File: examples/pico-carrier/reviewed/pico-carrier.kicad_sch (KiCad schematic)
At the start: 9 parts, among them J1 5V IN, J3 GP0-GP15, J4 GP16-GP28, PWR, U1 Pico

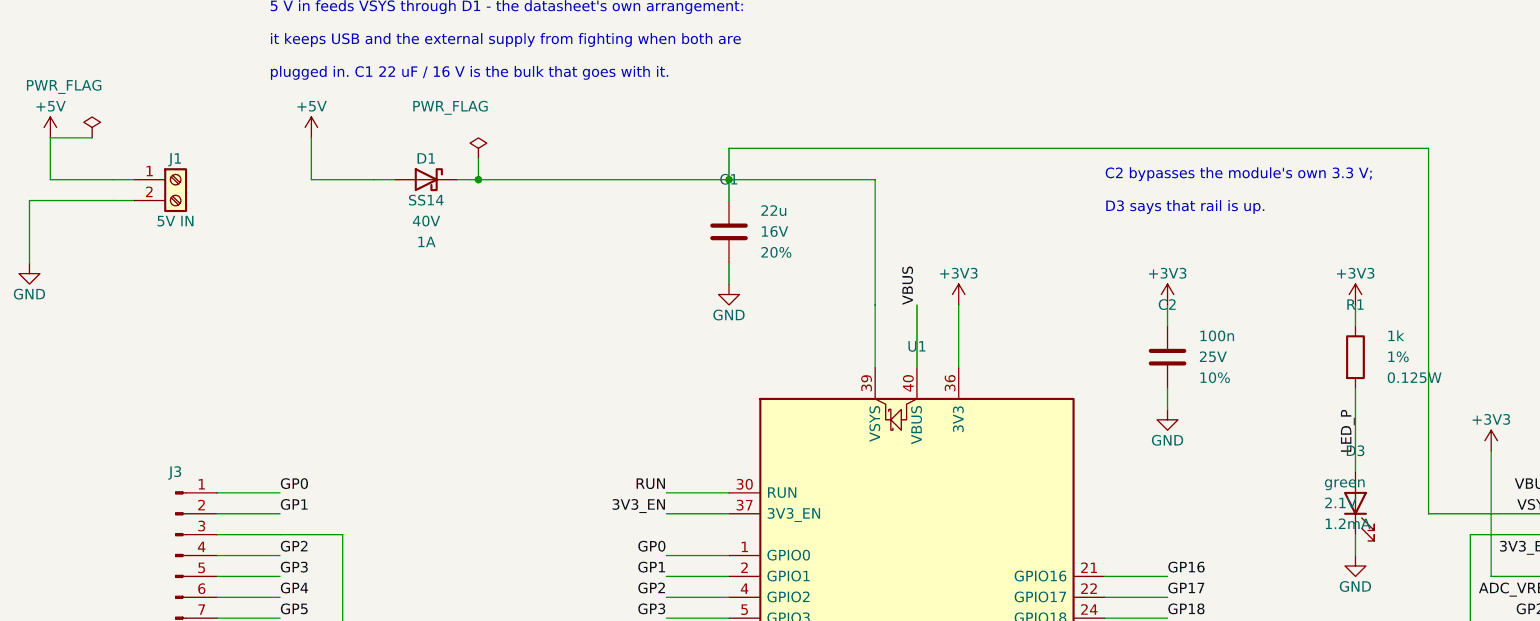
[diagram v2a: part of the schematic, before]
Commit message: Regenerate the four the text and width work changed
Designators and values off the rails they were printed on, power-named
nets at the width their rule asks for, and the buck's feedback ending
on the capacitor pad it senses at.

Co-Authored-By: Claude Fable 5 <noreply@anthropic.com>
Claude-Session: https://claude.ai/code/session_01DUj7Ltu92tWg159mCSacwY
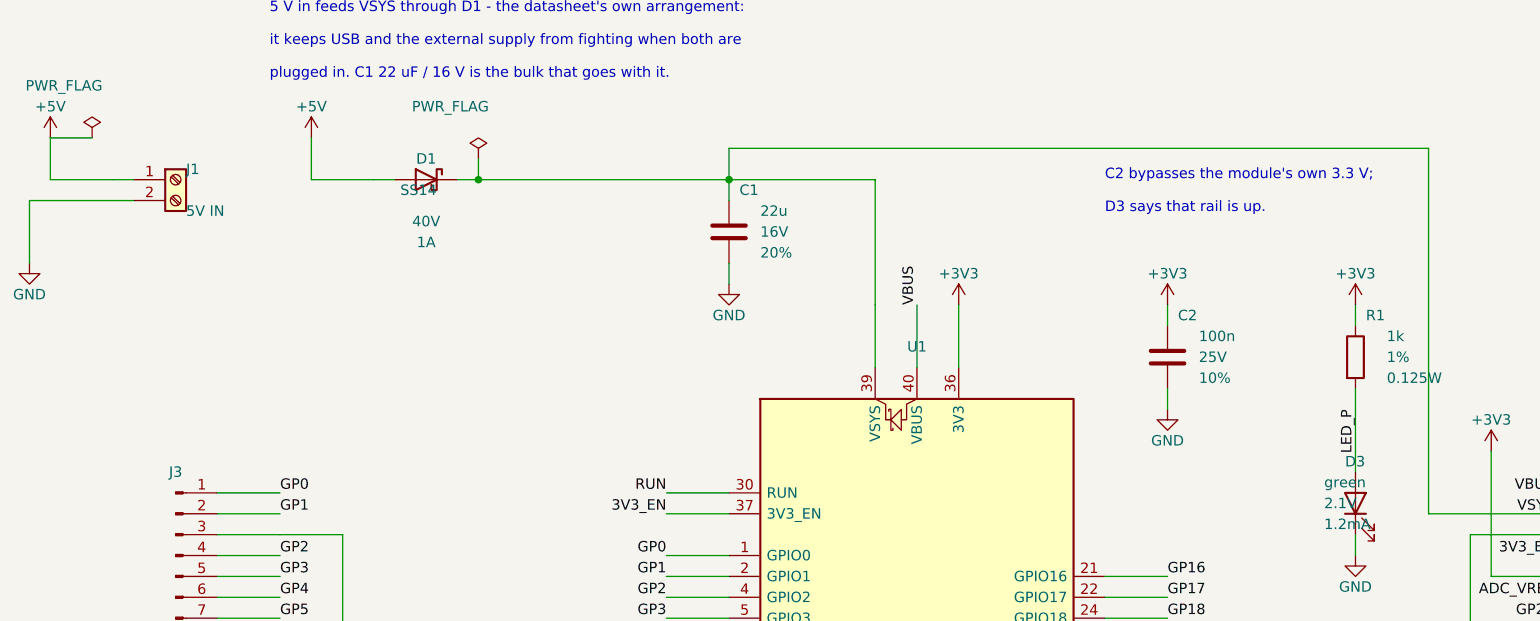
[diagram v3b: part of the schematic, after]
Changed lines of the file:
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@@
   (symbol (lib_id "Connector:Screw_Terminal_01x02") (at 59.69 39.37 0.0) (unit 1)
     (exclude_from_sim no) (in_bom yes) (on_board yes) (dnp no)
-    (property "Reference" "J1" (at 59.69 36.83 0) (effects (font (size 1.27 1.27))))
-    (property "Value" "5V IN" (at 59.69 44.45 0) (effects (font (size 1.27 1.27))))
+    (property "Reference" "J1" (at 60.96 38.1 0) (effects (font (size 1.27 1.27)) (justify left)))
+    (property "Value" "5V IN" (at 60.96 43.18 0) (effects (font (size 1.27 1.27)) (justify left)))
     (property "Footprint" "TerminalBlock_Phoenix:TerminalBlock_Phoenix_MKDS-1,5-2_1x02_P5.00mm_Horizontal" (at 59.69 39.37 0) (effects (font (size 1.27 1.27)) hide))
     (property "Datasheet" "https://www.phoenixcontact.com/product/1729128" (at 59.69 39.37 0) (effects (font (size 1.27 1.27)) hide))
@@
     (exclude_from_sim no) (in_bom yes) (on_board yes) (dnp no)
     (property "Reference" "D1" (at 90.17 36.83 0) (effects (font (size 1.27 1.27))))
-    (property "Value" "SS14" (at 90.17 41.91 0) (effects (font (size 1.27 1.27))))
+    (property "Value" "SS14" (at 91.44 40.64 0) (effects (font (size 1.27 1.27)) (justify left)))
     (property "Footprint" "Diode_SMD:D_SMA" (at 90.17 39.37 0) (effects (font (size 1.27 1.27)) hide))
     (property "Datasheet" "https://www.vishay.com/docs/88746/ss12.pdf" (at 90.17 39.37 0) (effects (font (size 1.27 1.27)) hide))
@@
   (symbol (lib_id "Device:C") (at 127.0 45.72 0.0) (unit 1)
     (exclude_from_sim no) (in_bom yes) (on_board yes) (dnp no)
-    (property "Reference" "C1" (at 127.0 39.37 0) (effects (font (size 1.27 1.27))))
+    (property "Reference" "C1" (at 128.27 40.64 0) (effects (font (size 1.27 1.27)) (justify left)))
     (property "Value" "22u" (at 130.81 43.18 0) (effects (font (size 1.27 1.27)) (justify left)))
     (property "Footprint" "Capacitor_SMD:C_1210_3225Metric" (at 127.0 45.72 0) (effects (font (size 1.27 1.27)) hide))
@@
   (symbol (lib_id "Device:C") (at 180.34 60.96 0.0) (unit 1)
     (exclude_from_sim no) (in_bom yes) (on_board yes) (dnp no)
-    (property "Reference" "C2" (at 180.34 54.61 0) (effects (font (size 1.27 1.27))))
+    (property "Reference" "C2" (at 181.61 55.88 0) (effects (font (size 1.27 1.27)) (justify left)))
     (property "Value" "100n" (at 184.15 58.42 0) (effects (font (size 1.27 1.27)) (justify left)))
     (property "Footprint" "Capacitor_SMD:C_0805_2012Metric" (at 180.34 60.96 0) (effects (font (size 1.27 1.27)) hide))
@@
   (symbol (lib_id "Device:R") (at 203.2 60.96 0.0) (unit 1)
     (exclude_from_sim no) (in_bom yes) (on_board yes) (dnp no)
-    (property "Reference" "R1" (at 203.2 54.61 0) (effects (font (size 1.27 1.27))))
+    (property "Reference" "R1" (at 204.47 55.88 0) (effects (font (size 1.27 1.27)) (justify left)))
     (property "Value" "1k" (at 207.01 58.42 0) (effects (font (size 1.27 1.27)) (justify left)))
     (property "Footprint" "Resistor_SMD:R_0805_2012Metric" (at 203.2 60.96 0) (effects (font (size 1.27 1.27)) hide))
@@
   (symbol (lib_id "Device:LED") (at 203.2 78.74 90.0) (unit 1)
     (exclude_from_sim no) (in_bom yes) (on_board yes) (dnp no)
-    (property "Reference" "D3" (at 203.2 72.39 90) (effects (font (size 1.27 1.27))))
+    (property "Reference" "D3" (at 201.93 73.66 90) (effects (font (size 1.27 1.27)) (justify right)))
     (property "Value" "green" (at 199.39 76.2 90) (effects (font (size 1.27 1.27)) (justify right)))
     (property "Footprint" "LED_SMD:LED_0805_2012Metric" (at 203.2 78.74 0) (effects (font (size 1.27 1.27)) hide))
